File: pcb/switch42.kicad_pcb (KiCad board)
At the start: 2 copper layers, 130.7 x 57.2 mm, 59 parts, among them J1 MJ-4PP-9, J2 MJ-4PP-9, SW1 SW_PUSH, SW10 SW_PUSH, SW11 SW_PUSH, SW12 SW_PUSH, SW13 SW_PUSH, SW14 SW_PUSH, SW15 SW_PUSH, SW16 SW_PUSH, SW17 SW_PUSH, SW18 SW_PUSH, SW19 SW_PUSH, SW2 SW_PUSH, SW20 SW_PUSH, SW21 SW_PUSH, SW22 SW_PUSH, SW23 SW_PUSH, SW24 SW_PUSH, SW25 SW_PUSH, SW26 SW_PUSH, SW27 SW_PUSH, SW28 SW_PUSH, SW29 SW_PUSH, SW3 SW_PUSH, SW30 SW_PUSH, SW31 SW_PUSH, SW32 SW_PUSH, SW33 SW_PUSH, SW34 SW_PUSH, SW35 SW_PUSH, SW36 SW_PUSH, SW37 SW_PUSH, SW4 SW_PUSH, SW5 SW_PUSH, SW6 SW_PUSH, SW7 SW_PUSH, SW8 SW_PUSH, SW9 SW_PUSH, U1 ProMicro

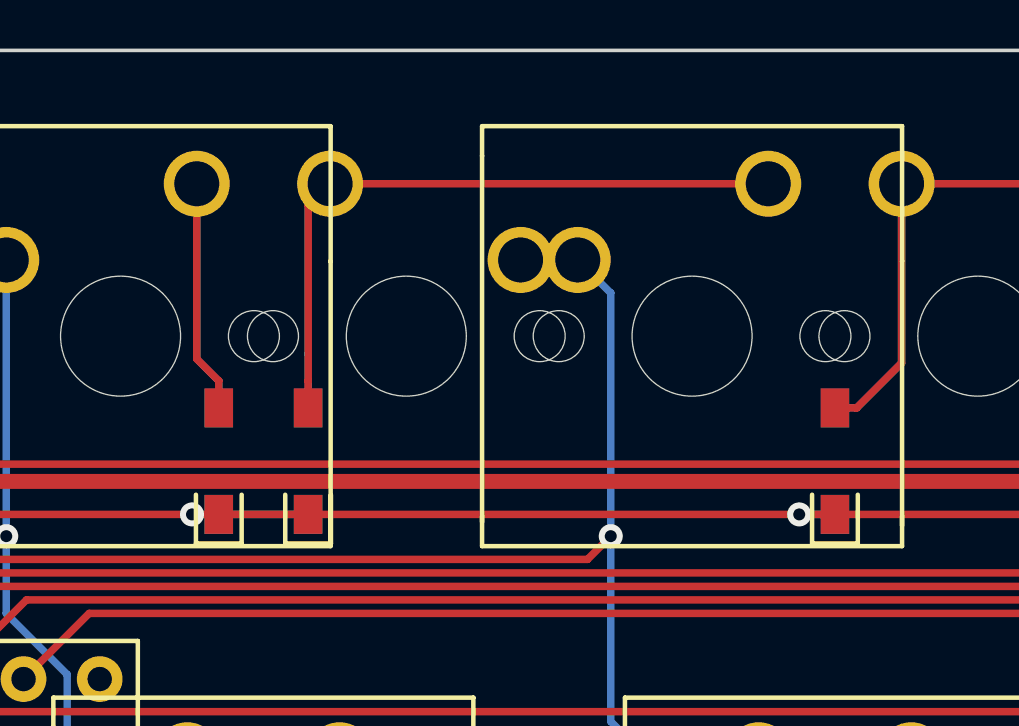
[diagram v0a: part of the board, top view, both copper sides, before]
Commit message: Adjust diode positions
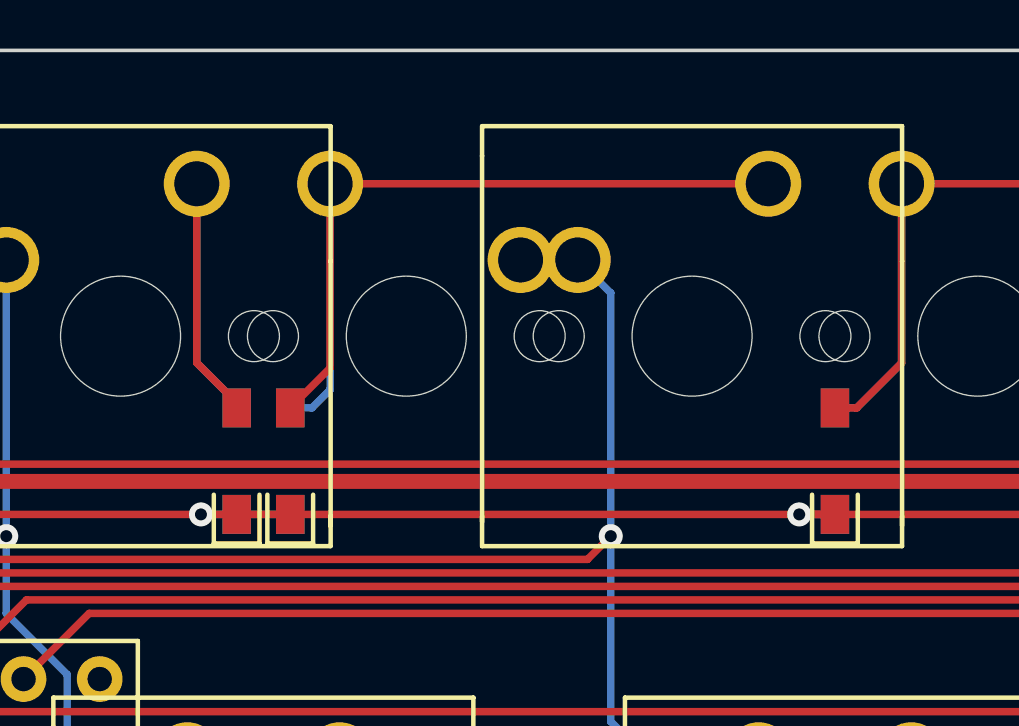
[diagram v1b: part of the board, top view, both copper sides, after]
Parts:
- moved D4 0.60 mm to (83.7, 48.7)
- moved D7 0.60 mm to (85.5, 48.7)
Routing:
- net Net-(D7-Pad2): track 30.2 -> 31.1 mm
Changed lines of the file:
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@@
     (thickness 1.2)
     (drawings 28)
-    (tracks 387)
+    (tracks 385)
     (zones 0)
     (modules 59)
@@
   )
   (module phi-kbd-library:D_SMD-reversible (layer F.Cu)
-    (at 83.08115 48.744212 90)
+    (at 83.676466 48.744212 90)
     (descr "Resitance 3 pas")
     (tags R)
@@
   )
   (module phi-kbd-library:D_SMD-reversible (layer F.Cu)
-    (at 86.05773 48.744212 90)
+    (at 85.462414 48.744212 90)
     (descr "Resitance 3 pas")
     (tags R)
@@
   (segment (start 70.754329 41.352999) (end 70.754329 42.721001) (width 0.25) (layer B.Cu) (net 1))
   (segment (start 63.2968 39.497) (end 68.89833 39.497) (width 0.25) (layer B.Cu) (net 1) (status 10))
-  (segment (start 83.08115 50.519212) (end 86.05773 50.519212) (width 0.25) (layer F.Cu) (net 2) (status 30))
   (segment (start 66.41219 70.169482) (end 66.41219 71.247112) (width 0.25) (layer B.Cu) (net 2))
   (segment (start 66.41219 63.460236) (end 66.41219 70.169482) (width 0.25) (layer B.Cu) (net 2))
@@
   (segment (start 63.138064 50.519212) (end 64.031038 50.519212) (width 0.25) (layer B.Cu) (net 2))
   (segment (start 63.138064 50.519212) (end 64.031038 50.519212) (width 0.25) (layer F.Cu) (net 2))
-  (segment (start 83.08115 50.519212) (end 86.05773 50.519212) (width 0.25) (layer B.Cu) (net 2))
-  (via (at 82.188176 50.519212) (size 0.8) (drill 0.4) (layers F.Cu B.Cu) (net 2))
-  (segment (start 83.08115 50.519212) (end 82.188176 50.519212) (width 0.25) (layer B.Cu) (net 2))
-  (segment (start 82.188176 50.519212) (end 83.08115 50.519212) (width 0.25) (layer F.Cu) (net 2))
   (segment (start 64.031038 50.519212) (end 82.188176 50.519212) (width 0.25) (layer F.Cu) (net 2))
   (via (at 102.42892 50.519212) (size 0.8) (drill 0.4) (layers F.Cu B.Cu) (net 2))
   (segment (start 102.42892 50.519212) (end 103.619552 50.519212) (width 0.25) (layer F.Cu) (net 2))
   (segment (start 103.619552 50.519212) (end 102.42892 50.519212) (width 0.25) (layer B.Cu) (net 2))
-  (segment (start 86.05773 50.519212) (end 102.42892 50.519212) (width 0.25) (layer F.Cu) (net 2))
   (via (at 121.479032 50.519212) (size 0.8) (drill 0.4) (layers F.Cu B.Cu) (net 2))
   (segment (start 121.479032 50.519212) (end 122.669664 50.519212) (width 0.25) (layer F.Cu) (net 2))
@@
   (segment (start 159.579256 50.519212) (end 160.769888 50.519212) (width 0.25) (layer F.Cu) (net 2))
   (segment (start 141.719776 50.519212) (end 159.579256 50.519212) (width 0.25) (layer F.Cu) (net 2))
+  (segment (start 83.676466 50.519212) (end 85.462414 50.519212) (width 0.25) (layer F.Cu) (net 2))
+  (segment (start 85.462414 50.519212) (end 103.619552 50.519212) (width 0.25) (layer F.Cu) (net 2))
+  (segment (start 83.676466 50.519212) (end 85.462414 50.519212) (width 0.25) (layer B.Cu) (net 2))
+  (segment (start 83.676466 50.519212) (end 82.485834 50.519212) (width 0.25) (layer B.Cu) (net 2))
+  (via (at 82.485834 50.519212) (size 0.8) (drill 0.4) (layers F.Cu B.Cu) (net 2))
+  (segment (start 82.485834 50.519212) (end 83.676466 50.519212) (width 0.25) (layer F.Cu) (net 2))
+  (segment (start 82.188176 50.519212) (end 82.485834 50.519212) (width 0.25) (layer F.Cu) (net 2))
   (segment (start 60.598064 58.547112) (end 65.678064 58.547112) (width 0.25) (layer F.Cu) (net 3) (status 30))
   (segment (start 79.974886 66.019324) (end 80.699886 66.019324) (width 0.25) (layer F.Cu) (net 3) (status 20))
@@
   (segment (start 131.301746 88.619436) (end 150.351858 88.619436) (width 0.25) (layer B.Cu) (net 6))
   (segment (start 150.351858 88.619436) (end 169.40197 88.619436) (width 0.25) (layer B.Cu) (net 6))
-  (segment (start 83.08115 46.069212) (end 83.08115 46.969212) (width 0.25) (layer F.Cu) (net 7) (status 20))
-  (segment (start 82.346912 45.334974) (end 83.08115 46.069212) (width 0.25) (layer F.Cu) (net 7))
-  (segment (start 82.346912 39.497) (end 82.346912 45.334974) (width 0.25) (layer F.Cu) (net 7) (status 10))
-  (segment (start 82.346912 39.497) (end 82.346912 45.331052) (width 0.25) (layer B.Cu) (net 7) (status 10))
-  (segment (start 83.08115 46.06529) (end 83.08115 46.969212) (width 0.25) (layer B.Cu) (net 7) (status 20))
-  (segment (start 82.346912 45.331052) (end 83.08115 46.06529) (width 0.25) (layer B.Cu) (net 7))
+  (segment (start 83.676466 46.794212) (end 83.676466 46.969212) (width 0.25) (layer B.Cu) (net 7))
+  (segment (start 82.346912 45.464658) (end 83.676466 46.794212) (width 0.25) (layer B.Cu) (net 7))
+  (segment (start 82.346912 39.497) (end 82.346912 45.464658) (width 0.25) (layer B.Cu) (net 7))
+  (segment (start 83.676466 46.794212) (end 83.676466 46.969212) (width 0.25) (layer F.Cu) (net 7))
+  (segment (start 82.346912 45.464658) (end 83.676466 46.794212) (width 0.25) (layer F.Cu) (net 7))
+  (segment (start 82.346912 39.497) (end 82.346912 45.464658) (width 0.25) (layer F.Cu) (net 7))
   (segment (start 82.02944 58.547112) (end 87.10944 58.547112) (width 0.25) (layer F.Cu) (net 8) (status 30))
   (segment (start 89.163994 66.019324) (end 88.438994 66.019324) (width 0.25) (layer F.Cu) (net 8) (status 20))
@@
   (segment (start 91.871968 77.597224) (end 92.971967 78.697223) (width 0.25) (layer B.Cu) (net 9))
   (segment (start 86.791968 39.497) (end 101.397024 39.497) (width 0.25) (layer F.Cu) (net 10) (status 30))
-  (segment (start 86.05773 46.069212) (end 86.05773 46.969212) (width 0.25) (layer F.Cu) (net 10) (status 20))
-  (segment (start 86.061913 46.065029) (end 86.05773 46.069212) (width 0.25) (layer F.Cu) (net 10))
-  (segment (start 86.061913 40.227055) (end 86.061913 46.065029) (width 0.25) (layer F.Cu) (net 10) (status 10))
-  (segment (start 86.791968 39.497) (end 86.061913 40.227055) (width 0.25) (layer F.Cu) (net 10) (status 30))
-  (segment (start 86.061913 40.227055) (end 86.061913 45.168133) (width 0.25) (layer B.Cu) (net 10) (status 10))
-  (segment (start 86.791968 39.497) (end 86.061913 40.227055) (width 0.25) (layer B.Cu) (net 10) (status 30))
-  (segment (start 86.05773 45.172316) (end 86.05773 46.969212) (width 0.25) (layer B.Cu) (net 10) (status 20))
-  (segment (start 86.061913 45.168133) (end 86.05773 45.172316) (width 0.25) (layer B.Cu) (net 10))
+  (segment (start 86.791968 45.639658) (end 85.462414 46.969212) (width 0.25) (layer F.Cu) (net 10))
+  (segment (start 86.791968 39.497) (end 86.791968 45.639658) (width 0.25) (layer F.Cu) (net 10))
+  (segment (start 86.791968 46.364658) (end 86.187414 46.969212) (width 0.25) (layer B.Cu) (net 10))
+  (segment (start 86.187414 46.969212) (end 85.462414 46.969212) (width 0.25) (layer B.Cu) (net 10))
+  (segment (start 86.791968 39.497) (end 86.791968 46.364658) (width 0.25) (layer B.Cu) (net 10))
   (segment (start 101.079552 58.547112) (end 106.159552 58.547112) (width 0.25) (layer F.Cu) (net 11) (status 30))
   (segment (start 108.214106 66.019324) (end 107.489106 66.019324) (width 0.25) (layer F.Cu) (net 11) (status 20))
